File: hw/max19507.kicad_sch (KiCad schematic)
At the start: 52 parts, among them U10 LMH6882, U8 THS4522, U9 MAX19507

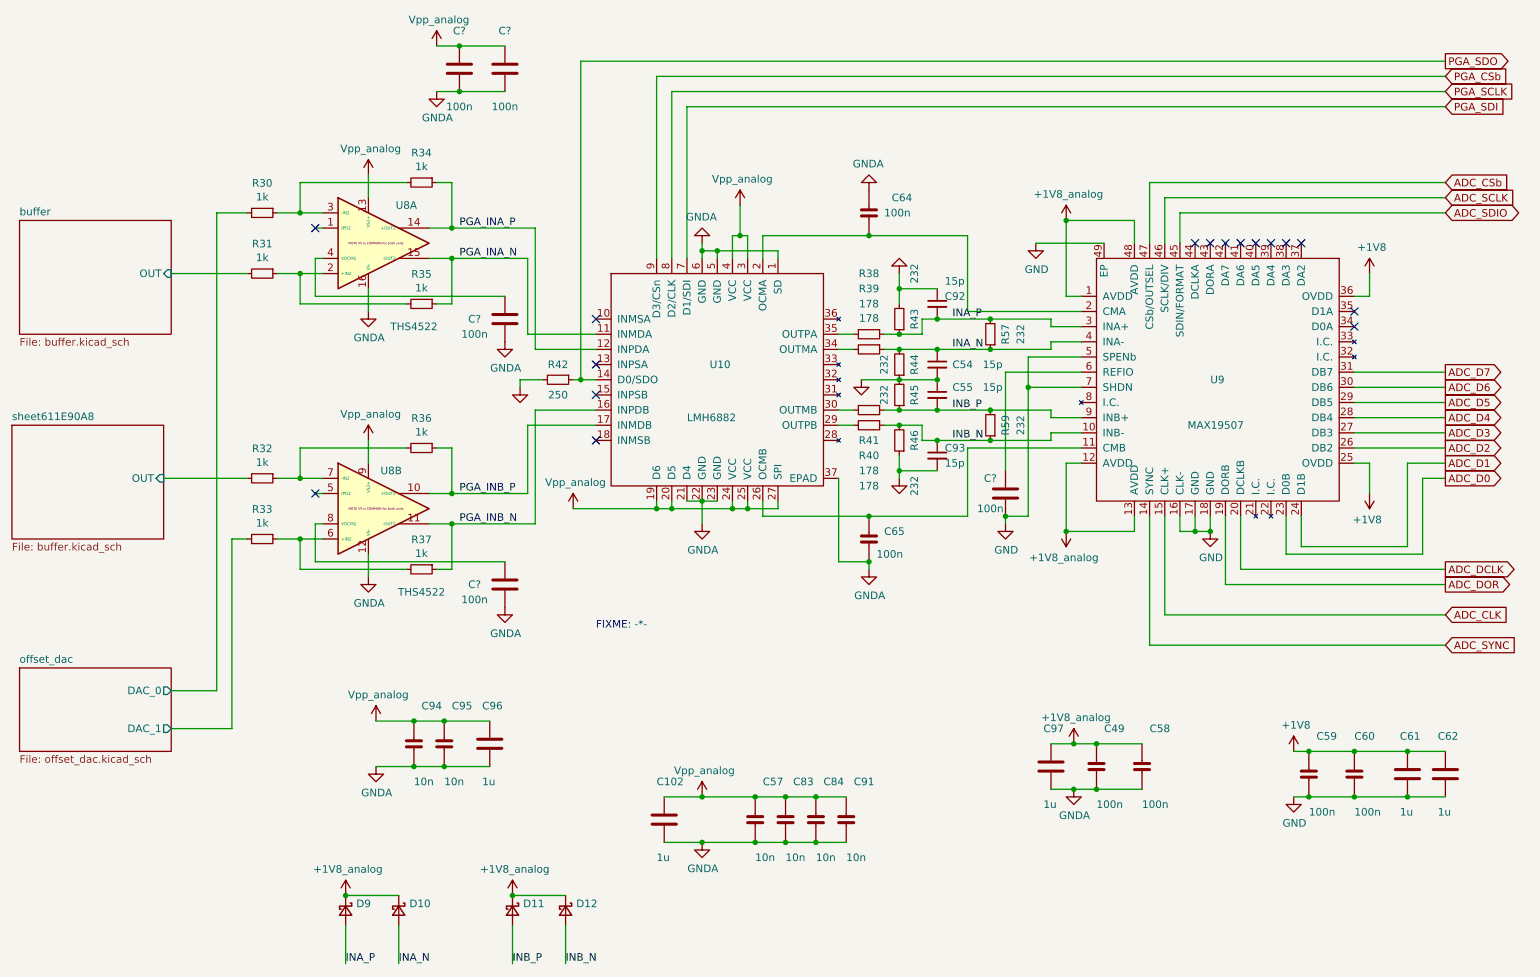
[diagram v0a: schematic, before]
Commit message: basic schematic, started layout (placing first components)
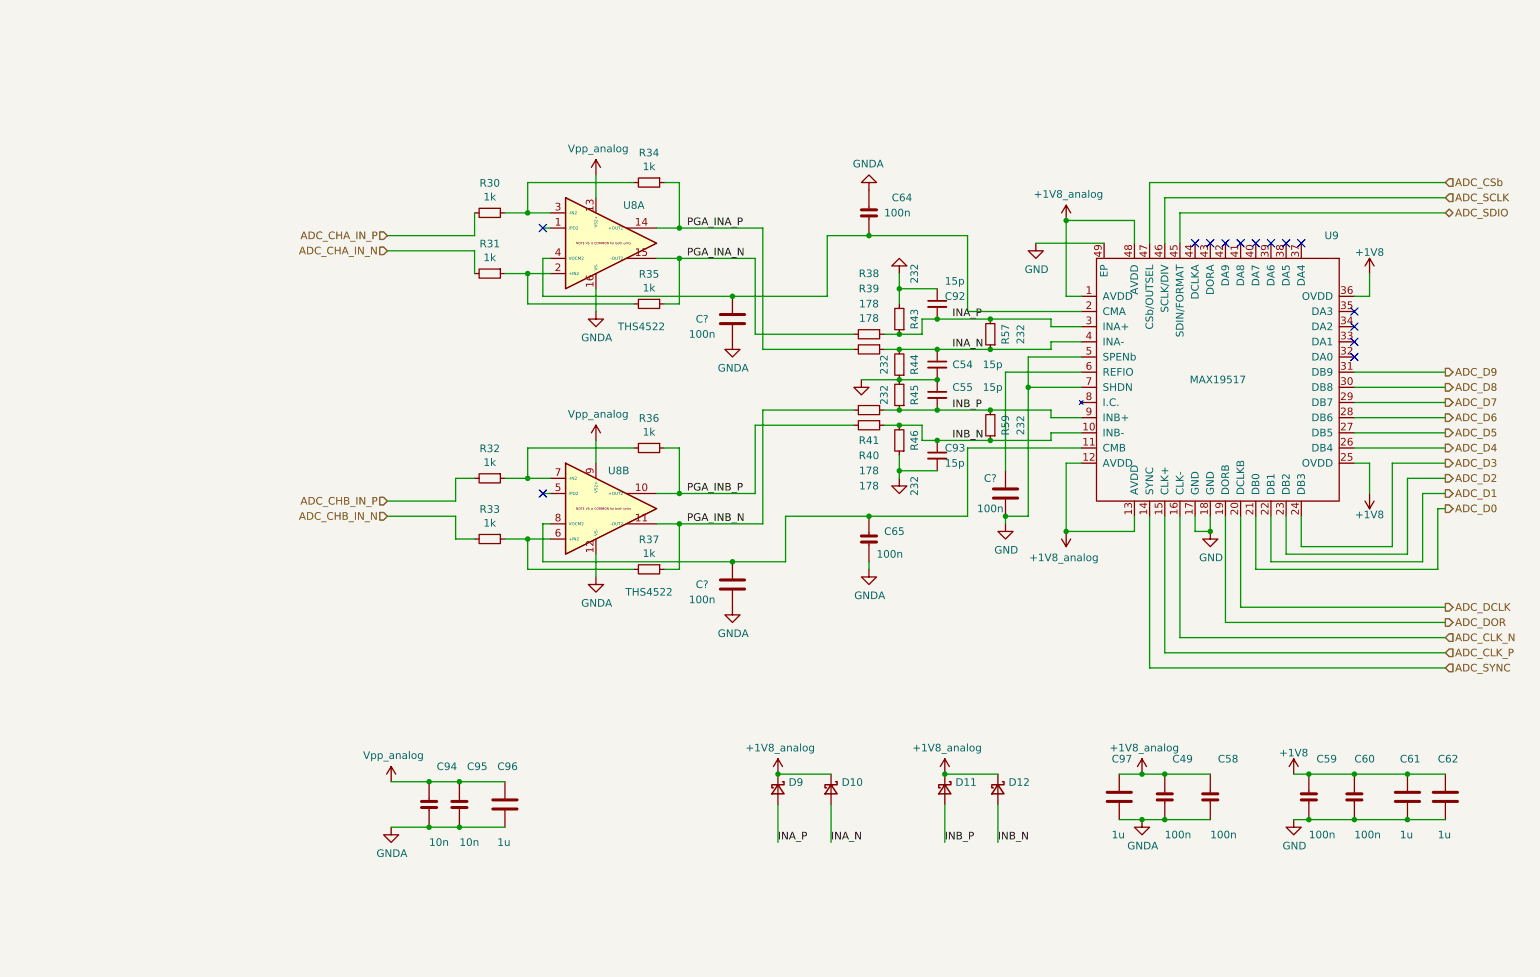
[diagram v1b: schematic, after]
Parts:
- removed C102: 1u, Capacitor_SMD:C_0805_2012Metric, symbol fmc:1uF_805
- removed C57, C83, C84, C91: 10n, Capacitor_SMD:C_0402_1005Metric, symbol fmc:100nF_402
- removed C? (x2): 100n, Capacitor_SMD:C_0603_1608Metric, symbol fmc:100nF_603
- removed R42: 250, Resistor_SMD:R_0603_1608Metric, symbol Device:R_Small
- removed U10: LMH6882, Package_DFN_QFN:Texas_S-PVQFN-N36_EP4.4x4.4mm_ThermalVias, symbol fmc:LMH6882
- removed U9: MAX19507, Package_QFP:TQFP-48-1EP_7x7mm_P0.5mm_EP5x5mm_ThermalVias, symbol fmc:MAX19507
- added U9: MAX19517, proj_footprints:QFN-48-1EP_7x7mm_P0.5mm_EP5.6x5.6mm_ThermalVias_biggerholes, symbol fmc:MAX19517
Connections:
- net +1V8: now also U9.25 (OVDD), U9.36 (OVDD)
- net +1V8_analog: now also U9.1 (AVDD), U9.12 (AVDD), U9.13 (AVDD), U9.48 (AVDD)
- net ADC_CSb: now also U9.47 (CSb/OUTSEL)
- net ADC_D0: now also U9.21 (DB0)
- net ADC_D1: now also U9.22 (DB1)
- net ADC_D2: now also U9.23 (DB2)
- net ADC_D3: now also U9.24 (DB3)
- net ADC_D4: now also U9.26 (DB4)
- net ADC_D5: now also U9.27 (DB5)
- net ADC_D6: now also U9.28 (DB6)
- net ADC_D7: now also U9.29 (DB7)
- net ADC_DCLK: now also U9.20 (DCLKB)
- net ADC_DOR: now also U9.19 (DORB)
- net ADC_SCLK: now also U9.46 (SCLK/DIV)
- net ADC_SDIO: now also U9.45 (SDIN/FORMAT)
- net ADC_SYNC: now also U9.14 (SYNC)
- net GND: now also U9.17 (GND), U9.18 (GND), U9.49 (EP), U9.5 (SPENb), U9.7 (SHDN)
- net INA_N: now also U9.4 (INA-)
- net INA_P: now also U9.3 (INA+)
- net INB_N: now also U9.10 (INB-)
- net INB_P: now also U9.9 (INB+)
- net PGA_INA_N: now also R38.2
- net PGA_INA_P: now also R39.2
- net PGA_INB_N: now also R40.2
- net PGA_INB_P: now also R41.2
- net at C64.2: now also C?.2, U8.4 (VOCM2), U9.2 (CMA)
- net at C65.1: now also C?.2, U8.8 (VOCM2), U9.11 (CMB)
- net at C?.2: now also U9.6 (REFIO)
- net buffer/OUT renamed ADC_CHA_IN_N
- net offset_dac/DAC_0 renamed ADC_CHA_IN_P
- net offset_dac/DAC_1 renamed ADC_CHB_IN_N
- net sheet611E90A8/OUT renamed ADC_CHB_IN_P
- new net ADC_CLK_N: U9.16 (CLK-)
- new net ADC_CLK_P: U9.15 (CLK+)
- new net ADC_D8: U9.30 (DB8)
- new net ADC_D9: U9.31 (DB9)
- no-connect marks 16 -> 14
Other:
- removed sheet buffer
- removed sheet offset_dac
- removed sheet sheet611E90A8
- note removed: "FIXME: -*-"
- moved on the sheet: C49, C58, C59, C60, C61, C62, C94, C95, C96, C97, C?, D10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

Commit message: WIP - a lot already laid out.
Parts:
- C94, C95: footprint Capacitor_SMD:C_0402_1005Metric -> Capacitor_SMD:C_0603_1608Metric
- R30, R31, R32, R33: footprint Resistor_SMD:R_0603_1608Metric -> Resistor_SMD:R_0402_1005Metric
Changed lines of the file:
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@@
       (effects (font (size 1.27 1.27)) (justify left))
     )
-    (property "Footprint" "Capacitor_SMD:C_0402_1005Metric" (at 93.6752 161.29 0)
+    (property "Footprint" "Capacitor_SMD:C_0603_1608Metric" (at 93.6752 161.29 0)
       (effects (font (size 1.27 1.27)) hide)
     )
@@
       (effects (font (size 1.27 1.27)) (justify left))
     )
-    (property "Footprint" "Capacitor_SMD:C_0402_1005Metric" (at 98.7552 161.29 0)
+    (property "Footprint" "Capacitor_SMD:C_0603_1608Metric" (at 98.7552 161.29 0)
       (effects (font (size 1.27 1.27)) hide)
     )
@@
       (effects (font (size 1.27 1.27)))
     )
-    (property "Footprint" "Resistor_SMD:R_0603_1608Metric" (at 102.87 58.42 0)
+    (property "Footprint" "Resistor_SMD:R_0402_1005Metric" (at 102.87 58.42 0)
       (effects (font (size 1.27 1.27)) hide)
     )
@@
       (effects (font (size 1.27 1.27)))
     )
-    (property "Footprint" "Resistor_SMD:R_0603_1608Metric" (at 102.87 68.58 0)
+    (property "Footprint" "Resistor_SMD:R_0402_1005Metric" (at 102.87 68.58 0)
       (effects (font (size 1.27 1.27)) hide)
     )
@@
       (effects (font (size 1.27 1.27)))
     )
-    (property "Footprint" "Resistor_SMD:R_0603_1608Metric" (at 102.87 102.87 0)
+    (property "Footprint" "Resistor_SMD:R_0402_1005Metric" (at 102.87 102.87 0)
       (effects (font (size 1.27 1.27)) hide)
     )
@@
       (effects (font (size 1.27 1.27)))
     )
-    (property "Footprint" "Resistor_SMD:R_0603_1608Metric" (at 102.87 113.03 0)
-      (effects (font (size 1.27 1.27)) hide)
-    )
+    (property "Footprint" "Resistor_SMD:R_0402_1005Metric" (at 102.87 113.03 0)
+      (effects (font (size 1.27 1.27)) hide)
+    )

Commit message: WIP - almost everything except power (converters) connected
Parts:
- C64, C65: footprint Capacitor_SMD:C_0402_1005Metric -> Capacitor_SMD:C_0603_1608Metric
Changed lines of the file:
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@@
       (effects (font (size 1.27 1.27)) (justify left))
     )
-    (property "Footprint" "Capacitor_SMD:C_0402_1005Metric" (at 167.3352 116.84 0)
+    (property "Footprint" "Capacitor_SMD:C_0603_1608Metric" (at 167.3352 116.84 0)
       (effects (font (size 1.27 1.27)) hide)
     )
@@
       (effects (font (size 1.27 1.27)) (justify left))
     )
-    (property "Footprint" "Capacitor_SMD:C_0402_1005Metric" (at 167.3352 62.23 0)
+    (property "Footprint" "Capacitor_SMD:C_0603_1608Metric" (at 167.3352 62.23 0)
       (effects (font (size 1.27 1.27)) hide)
     )

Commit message: finished routing; DRC passes (except for 1 hole violation at push-button)
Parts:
- C49, C58, C59, C60, C64, C65: Manufacturer Murata -> (none); Part GRM155R61C104KA88D -> (none)
- C61, C62, C96, C97: Manufacturer Murata -> (none); Part GCJ219R71C105KA01 -> (none)
- C94, C95: Manufacturer Murata -> (none); Part GRM155R61C103KA01 -> (none)
- C? (x3): Manufacturer Murata -> (none); Part GCJ188R71E104KA12D -> (none)
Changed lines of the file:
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@@
       (effects (font (size 1.27 1.27)) hide)
     )
-    (property "Part" "GRM155R61C104KA88D" (at 243.205 151.13 0)
-      (effects (font (size 1.27 1.27)) hide)
-    )
-    (property "Manufacturer" "Murata" (at 245.745 148.59 0)
+    (property "Part" "" (at 243.205 151.13 0)
+      (effects (font (size 1.27 1.27)) hide)
+    )
+    (property "Manufacturer" "" (at 245.745 148.59 0)
       (effects (font (size 1.27 1.27)) hide)
     )
@@
       (effects (font (size 1.27 1.27)) hide)
     )
-    (property "Part" "GRM155R61C104KA88D" (at 250.825 151.13 0)
-      (effects (font (size 1.27 1.27)) hide)
-    )
-    (property "Manufacturer" "Murata" (at 253.365 148.59 0)
+    (property "Part" "" (at 250.825 151.13 0)
+      (effects (font (size 1.27 1.27)) hide)
+    )
+    (property "Manufacturer" "" (at 253.365 148.59 0)
       (effects (font (size 1.27 1.27)) hide)
     )
@@
       (effects (font (size 1.27 1.27)) hide)
     )
-    (property "Part" "GRM155R61C103KA01" (at 95.885 152.4 0)
-      (effects (font (size 1.27 1.27)) hide)
-    )
-    (property "Manufacturer" "Murata" (at 98.425 149.86 0)
+    (property "Part" "" (at 95.885 152.4 0)
+      (effects (font (size 1.27 1.27)) hide)
+    )
+    (property "Manufacturer" "" (at 98.425 149.86 0)
       (effects (font (size 1.27 1.27)) hide)
     )
@@
       (effects (font (size 1.27 1.27)) hide)
     )
-    (property "Part" "GRM155R61C103KA01" (at 100.965 152.4 0)
-      (effects (font (size 1.27 1.27)) hide)
-    )
-    (property "Manufacturer" "Murata" (at 103.505 149.86 0)
+    (property "Part" "" (at 100.965 152.4 0)
+      (effects (font (size 1.27 1.27)) hide)
+    )
+    (property "Manufacturer" "" (at 103.505 149.86 0)
       (effects (font (size 1.27 1.27)) hide)
     )
@@
       (effects (font (size 1.27 1.27)) hide)
     )
-    (property "Part" "GRM155R61C104KA88D" (at 219.075 151.13 0)
-      (effects (font (size 1.27 1.27)) hide)
-    )
-    (property "Manufacturer" "Murata" (at 221.615 148.59 0)
+    (property "Part" "" (at 219.075 151.13 0)
+      (effects (font (size 1.27 1.27)) hide)
+    )
+    (property "Manufacturer" "" (at 221.615 148.59 0)
       (effects (font (size 1.27 1.27)) hide)
     )
@@
       (effects (font (size 1.27 1.27)) hide)
     )
-    (property "Part" "GRM155R61C104KA88D" (at 226.695 151.13 0)
-      (effects (font (size 1.27 1.27)) hide)
-    )
-    (property "Manufacturer" "Murata" (at 229.235 148.59 0)
+    (property "Part" "" (at 226.695 151.13 0)
+      (effects (font (size 1.27 1.27)) hide)
+    )
+    (property "Manufacturer" "" (at 229.235 148.59 0)
       (effects (font (size 1.27 1.27)) hide)
     )
@@
       (effects (font (size 1.27 1.27)) hide)
     )
-    (property "Part" "GCJ219R71C105KA01" (at 108.585 152.4 0)
-      (effects (font (size 1.27 1.27)) hide)
-    )
-    (property "Manufacturer" "Murata" (at 111.125 149.86 0)
+    (property "Part" "" (at 108.585 152.4 0)
+      (effects (font (size 1.27 1.27)) hide)
+    )
+    (property "Manufacturer" "" (at 111.125 149.86 0)
       (effects (font (size 1.27 1.27)) hide)
     )
@@
       (effects (font (size 1.27 1.27)) hide)
     )
-    (property "Part" "GCJ219R71C105KA01" (at 211.455 151.13 0)
-      (effects (font (size 1.27 1.27)) hide)
-    )
-    (property "Manufacturer" "Murata" (at 213.995 148.59 0)
+    (property "Part" "" (at 211.455 151.13 0)
+      (effects (font (size 1.27 1.27)) hide)
+    )
+    (property "Manufacturer" "" (at 213.995 148.59 0)
       (effects (font (size 1.27 1.27)) hide)
     )
@@
       (effects (font (size 1.27 1.27)) hide)
     )
-    (property "Part" "GRM155R61C104KA88D" (at 169.545 107.95 0)
-      (effects (font (size 1.27 1.27)) hide)
-    )
-    (property "Manufacturer" "Murata" (at 172.085 105.41 0)
+    (property "Part" "" (at 169.545 107.95 0)
+      (effects (font (size 1.27 1.27)) hide)
+    )
+    (property "Manufacturer" "" (at 172.085 105.41 0)
       (effects (font (size 1.27 1.27)) hide)
     )
@@
       (effects (font (size 1.27 1.27)) hide)
     )
-    (property "Part" "GRM155R61C104KA88D" (at 169.545 53.34 0)
-      (effects (font (size 1.27 1.27)) hide)
-    )
-    (property "Manufacturer" "Murata" (at 172.085 50.8 0)
+    (property "Part" "" (at 169.545 53.34 0)
+      (effects (font (size 1.27 1.27)) hide)
+    )
+    (property "Manufacturer" "" (at 172.085 50.8 0)
       (effects (font (size 1.27 1.27)) hide)
     )
@@
       (effects (font (size 1.27 1.27)) hide)
     )
-    (property "Part" "GCJ188R71E104KA12D" (at 140.335 81.28 0)
-      (effects (font (size 1.27 1.27)) hide)
-    )
-    (property "Manufacturer" "Murata" (at 137.795 83.82 0)
+    (property "Part" "" (at 140.335 81.28 0)
+      (effects (font (size 1.27 1.27)) hide)
+    )
+    (property "Manufacturer" "" (at 137.795 83.82 0)
       (effects (font (size 1.27 1.27)) hide)
     )
@@
       (effects (font (size 1.27 1.27)) hide)
     )
-    (property "Part" "GCJ188R71E104KA12D" (at 140.335 125.73 0)
-      (effects (font (size 1.27 1.27)) hide)
-    )
-    (property "Manufacturer" "Murata" (at 137.795 128.27 0)
+    (property "Part" "" (at 140.335 125.73 0)
+      (effects (font (size 1.27 1.27)) hide)
+    )
+    (property "Manufacturer" "" (at 137.795 128.27 0)
       (effects (font (size 1.27 1.27)) hide)
     )
@@
       (effects (font (size 1.27 1.27)) hide)
     )
-    (property "Part" "GCJ219R71C105KA01" (at 266.065 151.13 0)
-      (effects (font (size 1.27 1.27)) hide)
-    )
-    (property "Manufacturer" "Murata" (at 268.605 148.59 0)
+    (property "Part" "" (at 266.065 151.13 0)
+      (effects (font (size 1.27 1.27)) hide)
+    )
+    (property "Manufacturer" "" (at 268.605 148.59 0)
       (effects (font (size 1.27 1.27)) hide)
     )
@@
       (effects (font (size 1.27 1.27)) hide)
     )
-    (property "Part" "GCJ219R71C105KA01" (at 259.715 151.13 0)
-      (effects (font (size 1.27 1.27)) hide)
-    )
-    (property "Manufacturer" "Murata" (at 262.255 148.59 0)
+    (property "Part" "" (at 259.715 151.13 0)
+      (effects (font (size 1.27 1.27)) hide)
+    )
+    (property "Manufacturer" "" (at 262.255 148.59 0)
       (effects (font (size 1.27 1.27)) hide)
     )
@@
       (effects (font (size 1.27 1.27)) hide)
     )
-    (property "Part" "GCJ188R71E104KA12D" (at 186.055 110.49 0)
-      (effects (font (size 1.27 1.27)) hide)
-    )
-    (property "Manufacturer" "Murata" (at 183.515 113.03 0)
-      (effects (font (size 1.27 1.27)) hide)
-    )
+    (property "Part" "" (at 186.055 110.49 0)
+      (effects (font (size 1.27 1.27)) hide)
+    )
+    (property "Manufacturer" "" (at 183.515 113.03 0)
+      (effects (font (size 1.27 1.27)) hide)
+    )
